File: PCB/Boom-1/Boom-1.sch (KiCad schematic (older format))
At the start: 704 parts, among them J1 NoiseIOConn, J10 Osc1HFTrackConn, J11 Osc1FiltCVConn, J12 OscFiltEnv1Conn, J13 OscFiltEnv2Conn, J14 SubFiltEnv1Conn, J15 SubFiltEnv2Conn, J16 Osc1FXConn, J17 SubFXConn, J18 Osc1FiltCVConn, J19 Osc1FiltCVConn, J2 Conn_01x07, J20 Osc2FXConn, J21 OscAmpEnvConn, J22 SubAmpEnvConn, J23 OscAmpEnvBypass, J24 SubAmpAudioBypass, J25 SubAmpEnvBypass, J26 PreFV1FXConn, J27 PowerConn, J28 FV1Conn, J29 IOConn, J3 Osc1CVConn, J4 Osc2SyncConn, J5 Osc1SyncConn, J6 Osc2ScaleConn, J7 Osc2HFTrackConn, J8 Conn_01x03, J9 Osc1ScaleConn, Q1 2N3904, SW1 SW_DIP_x04, U1 CEM3340, U10 AS3320, U11 AS3310, U12 AS3310, U13 AS3310, U14 AS3310, U15 V2164D, U16 AS3310, U17 AS3310, U18 V2164D, U19 TL074, U2 CEM3340, U20 TL074, U21 TL072, U22 TL074, U23 TL074, U24 TL072, U25 TL074, U26 TL074, U27 TL072, U28 TL074, U29 TL072, U3 4013, U30 TL074, U31 TL072, U32 TL074, U33 TL074, U34 TL074, U35 TL072, U36 TL074, U37 TL074, U38 TL072, U39 TL074, U4 NOISE, U40 TL072, U41 TL074, U42 TL074, U43 TL074, U44 TL074, U45 L7905, U46 L7805, U47 TL072, U48 TL072, U5 V2164D, U6 V2164D, U7 V2164D, U8 AS3320, U9 AS3320

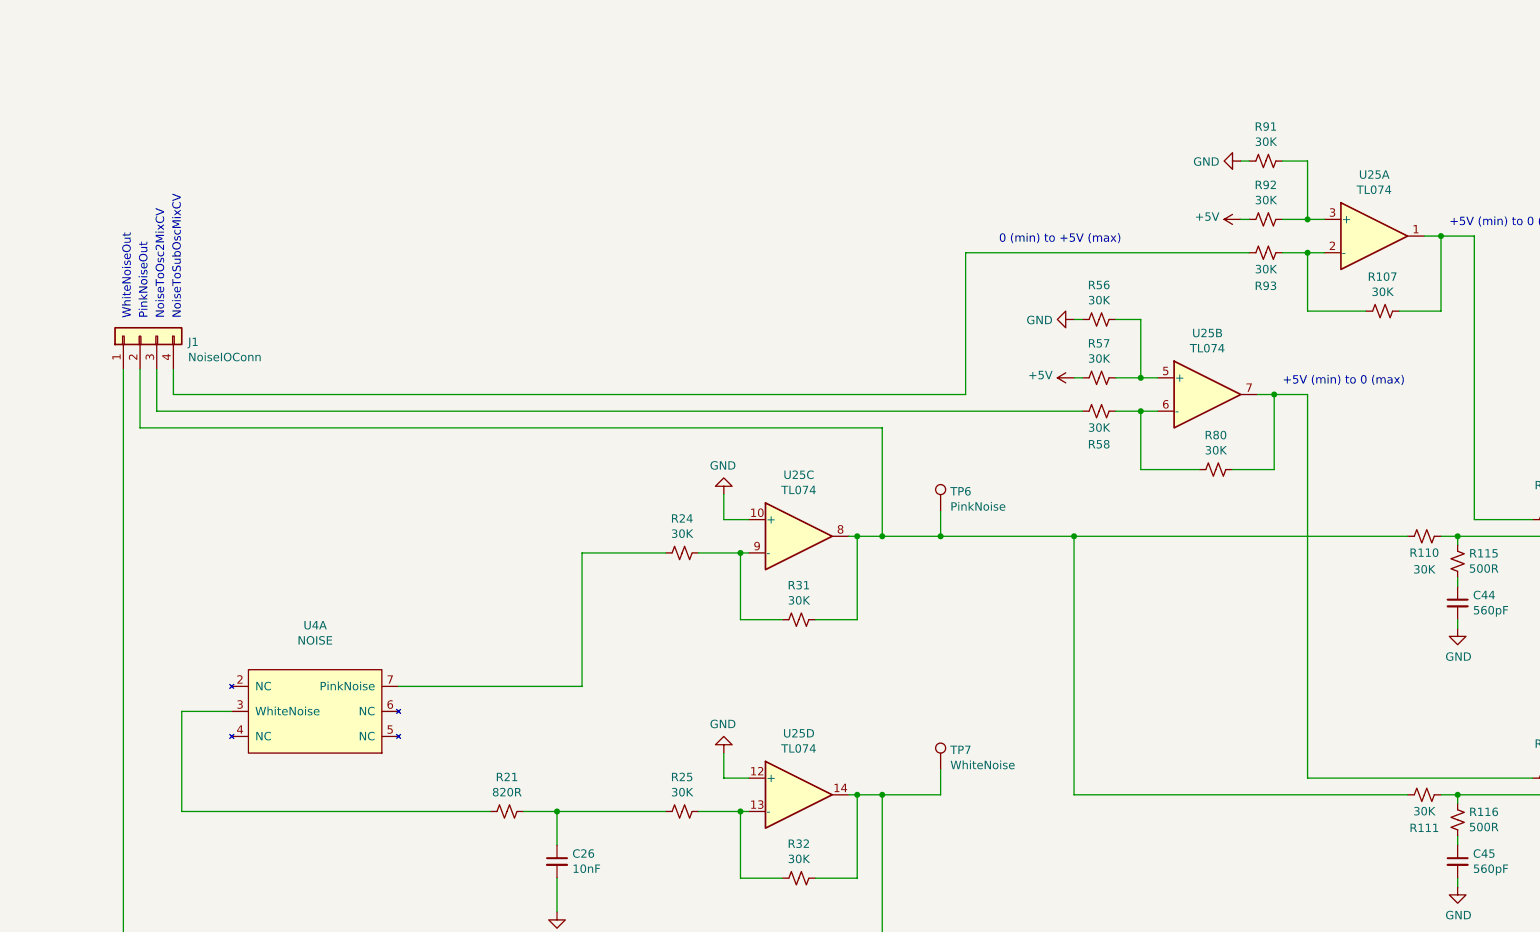
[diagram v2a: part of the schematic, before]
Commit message: compacted osc1, osc2, sub and noise
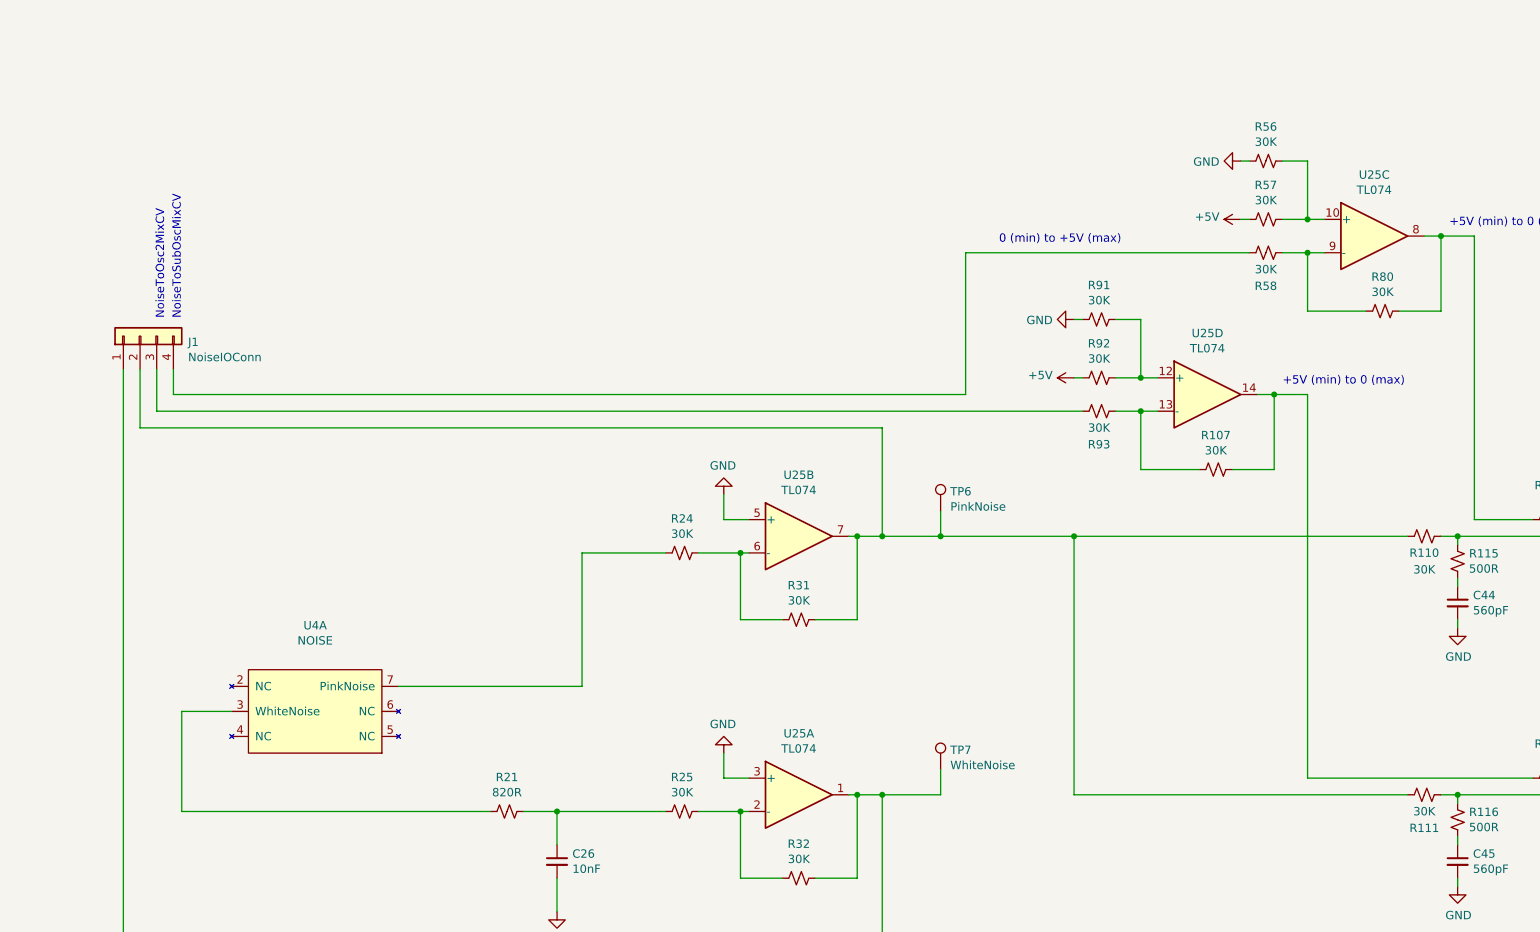
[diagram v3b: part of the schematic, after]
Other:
- note removed: "PinkNoiseOut"
- note removed: "WhiteNoiseOut"
- moved on the sheet: R107, R56, R57, R58, R80, R91, R92, R93
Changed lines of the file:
@@
 Connection ~ 10450 47750
 Wire Wire Line
-	10450 49300 10600 49300
-Wire Wire Line
 	10450 47750 10600 47750
 $Comp
@@
 Wire Wire Line
 	10600 47750 10950 47750
-Text Notes 6200 46450 1    50   ~ 0
-PinkNoiseOut
-Text Notes 6100 46450 1    50   ~ 0
-WhiteNoiseOut
 Text Notes 6300 46450 1    50   ~ 0
 NoiseToOsc2MixCV
@@
 	10550 43750 10700 43750
 Wire Wire Line
-	6050 50300 10600 50300
-Wire Wire Line
-	10600 50300 10600 49300
-Connection ~ 10600 49300
-Wire Wire Line
-	10600 49300 10950 49300
-Wire Wire Line
 	16000 47700 16500 47700
 Wire Wire Line
@@
 Wire Wire Line
 	6150 47100 10600 47100
-Wire Wire Line
-	6050 46750 6050 50300
 Text Label 35350 28950 0    50   ~ 0
 AudioOutput
@@
 	12950 46900 13150 46900
 Wire Wire Line
-	12150 46450 12150 46800
+	13150 45500 13150 45850
 Wire Wire Line
-	12150 46450 12000 46450
+	13150 45500 13000 45500
 $Comp
 L Device:R_Small_US R56
 U 1 1 770F3747
-P 11900 46450
-F 0 "R56" V 12105 46450 50  0000 C CNN
-F 1 "30K" V 12014 46450 50  0000 C CNN
-F 2 "Resistor_THT:R_Axial_DIN0207_L6.3mm_D2.5mm_P7.62mm_Horizontal" H 11900 46450 50  0001 C CNN
-F 3 "~" H 11900 46450 50  0001 C CNN
-	1    11900 46450
+P 12900 45500
+F 0 "R56" V 13105 45500 50  0000 C CNN
+F 1 "30K" V 13014 45500 50  0000 C CNN
+F 2 "Resistor_THT:R_Axial_DIN0207_L6.3mm_D2.5mm_P7.62mm_Horizontal" H 12900 45500 50  0001 C CNN
+F 3 "~" H 12900 45500 50  0001 C CNN
+	1    12900 45500
 	0    -1   -1   0
 $EndComp
 Wire Wire Line
-	12150 46800 12250 46800
-Connection ~ 12150 46800
+	13150 45850 13250 45850
+Connection ~ 13150 45850
 Wire Wire Line
 	11800 46800 11750 46800
 Wire Wire Line
-	12000 46800 12150 46800
+	13000 45850 13150 45850
 $Comp
 L Device:R_Small_US R57
 U 1 1 770F372B
-P 11900 46800
-F 0 "R57" V 12105 46800 50  0000 C CNN
-F 1 "30K" V 12014 46800 50  0000 C CNN
-F 2 "Resistor_THT:R_Axial_DIN0207_L6.3mm_D2.5mm_P7.62mm_Horizontal" H 11900 46800 50  0001 C CNN
-F 3 "~" H 11900 46800 50  0001 C CNN
-	1    11900 46800
+P 12900 45850
+F 0 "R57" V 13105 45850 50  0000 C CNN
+F 1 "30K" V 13014 45850 50  0000 C CNN
+F 2 "Resistor_THT:R_Axial_DIN0207_L6.3mm_D2.5mm_P7.62mm_Horizontal" H 12900 45850 50  0001 C CNN
+F 3 "~" H 12900 45850 50  0001 C CNN
+	1    12900 45850
 	0    -1   -1   0
 $EndComp
-Connection ~ 12150 47000
+Connection ~ 13150 46050
 Wire Wire Line
-	12000 47000 12150 47000
+	13000 46050 13150 46050
 $Comp
 L Device:R_Small_US R58
 U 1 1 770F3711
-P 11900 47000
-F 0 "R58" V 11700 47000 50  0000 C CNN
-F 1 "30K" V 11800 47000 50  0000 C CNN
-F 2 "Resistor_THT:R_Axial_DIN0207_L6.3mm_D2.5mm_P7.62mm_Horizontal" H 11900 47000 50  0001 C CNN
-F 3 "~" H 11900 47000 50  0001 C CNN
-	1    11900 47000
+P 12900 46050
+F 0 "R58" V 12700 46050 50  0000 C CNN
+F 1 "30K" V 12800 46050 50  0000 C CNN
+F 2 "Resistor_THT:R_Axial_DIN0207_L6.3mm_D2.5mm_P7.62mm_Horizontal" H 12900 46050 50  0001 C CNN
+F 3 "~" H 12900 46050 50  0001 C CNN
+	1    12900 46050
 	0    -1   -1   0
 $EndComp
 Wire Wire Line
-	12950 47350 12700 47350
+	13950 46400 13700 46400
 Wire Wire Line
 	12950 46900 12950 47350
@@
 	12850 46900 12950 46900
 Wire Wire Line
-	12150 47350 12500 47350
+	13150 46400 13500 46400
 Wire Wire Line
-	12150 47000 12150 47350
+	13150 46050 13150 46400
 Wire Wire Line
-	12250 47000 12150 47000
+	13250 46050 13150 46050
 $Comp
 L Device:R_Small_US R80
 U 1 1 770F36F3
-P 12600 47350
-F 0 "R80" V 12805 47350 50  0000 C CNN
-F 1 "30K" V 12714 47350 50  0000 C CNN
-F 2 "Resistor_THT:R_Axial_DIN0207_L6.3mm_D2.5mm_P7.62mm_Horizontal" H 12600 47350 50  0001 C CNN
-F 3 "~" H 12600 47350 50  0001 C CNN
-	1    12600 47350
+P 13600 46400
+F 0 "R80" V 13805 46400 50  0000 C CNN
+F 1 "30K" V 13714 46400 50  0000 C CNN
+F 2 "Resistor_THT:R_Axial_DIN0207_L6.3mm_D2.5mm_P7.62mm_Horizontal" H 13600 46400 50  0001 C CNN
+F 3 "~" H 13600 46400 50  0001 C CNN
+	1    13600 46400
 	0    -1   -1   0
 $EndComp
-Connection ~ 13950 45950
 Wire Wire Line
 	13950 45950 14150 45950
@@
 $EndComp
 Wire Wire Line
-	13150 45500 13150 45850
+	12150 46450 12150 46800
 Wire Wire Line
-	13150 45500 13000 45500
+	12150 46450 12000 46450
 $Comp
 L Device:R_Small_US R91
 U 1 1 770F3660
-P 12900 45500
-F 0 "R91" V 13105 45500 50  0000 C CNN
-F 1 "30K" V 13014 45500 50  0000 C CNN
-F 2 "Resistor_THT:R_Axial_DIN0207_L6.3mm_D2.5mm_P7.62mm_Horizontal" H 12900 45500 50  0001 C CNN
-F 3 "~" H 12900 45500 50  0001 C CNN
-	1    12900 45500
+P 11900 46450
+F 0 "R91" V 12105 46450 50  0000 C CNN
+F 1 "30K" V 12014 46450 50  0000 C CNN
+F 2 "Resistor_THT:R_Axial_DIN0207_L6.3mm_D2.5mm_P7.62mm_Horizontal" H 11900 46450 50  0001 C CNN
+F 3 "~" H 11900 46450 50  0001 C CNN
+	1    11900 46450
 	0    -1   -1   0
 $EndComp
 Wire Wire Line
-	13150 45850 13250 45850
-Connection ~ 13150 45850
+	12150 46800 12250 46800
+Connection ~ 12150 46800
 Wire Wire Line
 	12800 45850 12750 45850
@@
 $EndComp
 Wire Wire Line
-	13000 45850 13150 45850
+	12000 46800 12150 46800
 $Comp
 L Device:R_Small_US R92
 U 1 1 770F362E
-P 12900 45850
-F 0 "R92" V 13105 45850 50  0000 C CNN
-F 1 "30K" V 13014 45850 50  0000 C CNN
-F 2 "Resistor_THT:R_Axial_DIN0207_L6.3mm_D2.5mm_P7.62mm_Horizontal" H 12900 45850 50  0001 C CNN
-F 3 "~" H 12900 45850 50  0001 C CNN
-	1    12900 45850
+P 11900 46800
+F 0 "R92" V 12105 46800 50  0000 C CNN
+F 1 "30K" V 12014 46800 50  0000 C CNN
+F 2 "Resistor_THT:R_Axial_DIN0207_L6.3mm_D2.5mm_P7.62mm_Horizontal" H 11900 46800 50  0001 C CNN
+F 3 "~" H 11900 46800 50  0001 C CNN
+	1    11900 46800
 	0    -1   -1   0
 $EndComp
-Connection ~ 13150 46050
+Connection ~ 12150 47000
 Wire Wire Line
-	13000 46050 13150 46050
+	12000 47000 12150 47000
 $Comp
 L Device:R_Small_US R93
 U 1 1 770F3614
-P 12900 46050
-F 0 "R93" V 12700 46050 50  0000 C CNN
-F 1 "30K" V 12800 46050 50  0000 C CNN
-F 2 "Resistor_THT:R_Axial_DIN0207_L6.3mm_D2.5mm_P7.62mm_Horizontal" H 12900 46050 50  0001 C CNN
-F 3 "~" H 12900 46050 50  0001 C CNN
-	1    12900 46050
+P 11900 47000
+F 0 "R93" V 11700 47000 50  0000 C CNN
+F 1 "30K" V 11800 47000 50  0000 C CNN
+F 2 "Resistor_THT:R_Axial_DIN0207_L6.3mm_D2.5mm_P7.62mm_Horizontal" H 11900 47000 50  0001 C CNN
+F 3 "~" H 11900 47000 50  0001 C CNN
+	1    11900 47000
 	0    -1   -1   0
 $EndComp
 Wire Wire Line
-	13950 46400 13700 46400
+	12950 47350 12700 47350
 Wire Wire Line
 	13950 45950 13950 46400
 Wire Wire Line
-	13850 45950 13950 45950
-Wire Wire Line
-	13150 46400 13500 46400
+	12150 47350 12500 47350
 Wire Wire Line
-	13150 46050 13150 46400
+	12150 47000 12150 47350
 Wire Wire Line
-	13250 46050 13150 46050
+	12250 47000 12150 47000
 $Comp
 L Device:R_Small_US R107
 U 1 1 770F35F6
-P 13600 46400
-F 0 "R107" V 13805 46400 50  0000 C CNN
-F 1 "30K" V 13714 46400 50  0000 C CNN
-F 2 "Resistor_THT:R_Axial_DIN0207_L6.3mm_D2.5mm_P7.62mm_Horizontal" H 13600 46400 50  0001 C CNN
-F 3 "~" H 13600 46400 50  0001 C CNN
-	1    13600 46400
+P 12600 47350
+F 0 "R107" V 12805 47350 50  0000 C CNN
+F 1 "30K" V 12714 47350 50  0000 C CNN
+F 2 "Resistor_THT:R_Axial_DIN0207_L6.3mm_D2.5mm_P7.62mm_Horizontal" H 12600 47350 50  0001 C CNN
+F 3 "~" H 12600 47350 50  0001 C CNN
+	1    12600 47350
 	0    -1   -1   0
 $EndComp
@@
 $Comp
 L Amplifier_Operational:TL074 U25
-U 1 1 69F139BD
-P 13550 45950
-F 0 "U25" H 13550 46317 50  0000 C CNN
-F 1 "TL074" H 13550 46226 50  0000 C CNN
-F 2 "Package_DIP:DIP-14_W7.62mm" H 13500 46050 50  0001 C CNN
-F 3 "http://www.ti.com/lit/ds/symlink/tl071.pdf" H 13600 46150 50  0001 C CNN
-	1    13550 45950
-	1    0    0    -1
-$EndComp
-$Comp
-L Amplifier_Operational:TL074 U25
-U 2 1 69F1B5EF
+U 4 1 69F139BD
 P 12550 46900
 F 0 "U25" H 12550 47267 50  0000 C CNN
@@
 F 2 "Package_DIP:DIP-14_W7.62mm" H 12500 47000 50  0001 C CNN
 F 3 "http://www.ti.com/lit/ds/symlink/tl071.pdf" H 12600 47100 50  0001 C CNN
-	2    12550 46900
+	4    12550 46900
+	1    0    0    -1
+$EndComp
+$Comp
+L Amplifier_Operational:TL074 U25
+U 3 1 69F1B5EF
+P 13550 45950
+F 0 "U25" H 13550 46317 50  0000 C CNN
+F 1 "TL074" H 13550 46226 50  0000 C CNN
+F 2 "Package_DIP:DIP-14_W7.62mm" H 13500 46050 50  0001 C CNN
+F 3 "http://www.ti.com/lit/ds/symlink/tl071.pdf" H 13600 46150 50  0001 C CNN
+	3    13550 45950
 	1    0    0    -1
 $EndComp
 $Comp
 L Amplifier_Operational:TL074 U25
-U 3 1 69F235EB
+U 2 1 69F235EB
 P 10100 47750
 F 0 "U25" H 10100 48117 50  0000 C CNN
@@
 F 2 "Package_DIP:DIP-14_W7.62mm" H 10050 47850 50  0001 C CNN
 F 3 "http://www.ti.com/lit/ds/symlink/tl071.pdf" H 10150 47950 50  0001 C CNN
-	3    10100 47750
+	2    10100 47750
 	1    0    0    -1
 $EndComp
 $Comp
 L Amplifier_Operational:TL074 U25
-U 4 1 69F2BE9E
+U 1 1 69F2BE9E
 P 10100 49300
 F 0 "U25" H 10100 49667 50  0000 C CNN
@@
 F 2 "Package_DIP:DIP-14_W7.62mm" H 10050 49400 50  0001 C CNN
 F 3 "http://www.ti.com/lit/ds/symlink/tl071.pdf" H 10150 49500 50  0001 C CNN
-	4    10100 49300
+	1    10100 49300
 	1    0    0    -1
 $EndComp
@@
 Wire Wire Line
 	12850 32900 12850 35250
+Wire Wire Line
+	10600 49300 10950 49300
+Wire Wire Line
+	10450 49300 10600 49300
+Connection ~ 10600 49300
+Wire Wire Line
+	10600 50300 10600 49300
+Wire Wire Line
+	6050 50300 10600 50300
+Wire Wire Line
+	6050 46750 6050 50300
+Wire Wire Line
+	13850 45950 13950 45950
+Connection ~ 13950 45950
 $EndSCHEMATC

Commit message: osc2 filt layout WITHOUT VIA .. BOOM
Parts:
- removed J19: Osc1FiltCVConn, Connector_PinHeader_2.54mm:PinHeader_1x02_P2.54mm_Vertical, symbol Connector_Generic:Conn_01x02
- removed J20: Osc2FXConn, Connector_PinHeader_2.54mm:PinHeader_1x05_P2.54mm_Vertical, symbol Connector_Generic:Conn_01x05
- removed U30: TL074, Package_DIP:DIP-14_W7.62mm, symbol Amplifier_Operational:TL074
- added C180, C181: 100nF, Capacitor_THT:C_Disc_D5.0mm_W2.5mm_P5.00mm, symbol Device:C_Small
- added J20: Osc2FXConn, Connector_PinHeader_2.54mm:PinHeader_1x07_P2.54mm_Vertical, symbol Connector_Generic:Conn_01x07
- added U30, U49: TL072, Package_DIP:DIP-8_W7.62mm, symbol Amplifier_Operational:TL072
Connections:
- wire segments 3049 -> 3061

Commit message: updated conns on osc1 and sub filt to match osc2 filt
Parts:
- removed J11, J18: Osc1FiltCVConn, Connector_PinHeader_2.54mm:PinHeader_1x02_P2.54mm_Vertical, symbol Connector_Generic:Conn_01x02
- removed J16: Osc1FXConn, Connector_PinHeader_2.54mm:PinHeader_1x05_P2.54mm_Vertical, symbol Connector_Generic:Conn_01x05
- removed J17: SubFXConn, Connector_PinHeader_2.54mm:PinHeader_1x05_P2.54mm_Vertical, symbol Connector_Generic:Conn_01x05
- added J11: SubFiltConn, Connector_PinHeader_2.54mm:PinHeader_1x07_P2.54mm_Vertical, symbol Connector_Generic:Conn_01x07
- added J16: Osc1FiltConn, Connector_PinHeader_2.54mm:PinHeader_1x07_P2.54mm_Vertical, symbol Connector_Generic:Conn_01x07
- J20: value Osc2FXConn -> Osc2FiltConn
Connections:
- wire segments 3061 -> 3065
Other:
- moved on the sheet: TP27, TP30

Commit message: almost done with a filt env layout
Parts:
- removed J12: OscFiltEnv1Conn, Connector_PinHeader_2.54mm:PinHeader_1x10_P2.54mm_Vertical, symbol Connector_Generic:Conn_01x10
- added J12: OscFiltEnv1Conn, Connector_PinHeader_2.54mm:PinHeader_1x05_P2.54mm_Vertical, symbol Connector_Generic:Conn_01x05
- added J17: OscFiltEnv1CVConn, Connector_PinHeader_2.54mm:PinHeader_1x04_P2.54mm_Vertical, symbol Connector_Generic:Conn_01x04
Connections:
- no-connect marks 19 -> 18
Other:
- moved on the sheet: U27A, U27B
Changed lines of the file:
@@
 Text Notes 20750 21100 3    50   ~ 0
 OscFiltEnv1Trigger
-Text Notes 20850 21100 3    50   ~ 0
+Text Notes 20900 21100 3    50   ~ 0
 OscFiltEnv1AttackCV
-Text Notes 20950 21100 3    50   ~ 0
+Text Notes 21000 21100 3    50   ~ 0
 OscFiltEnv1DecayCV
-Text Notes 21050 21100 3    50   ~ 0
+Text Notes 21100 21100 3    50   ~ 0
 OscFiltEnv1SustainCV
-Text Notes 21150 21100 3    50   ~ 0
+Text Notes 21200 21100 3    50   ~ 0
 OscFiltEnv1ReleaseCV
-$Comp
-L Connector_Generic:Conn_01x10 J12
-U 1 1 732F368F
-P 20750 21000
-F 0 "J12" V 20800 20350 50  0000 C CNN
-F 1 "OscFiltEnv1Conn" V 20700 20100 50  0000 C CNN
-F 2 "Connector_PinHeader_2.54mm:PinHeader_1x10_P2.54mm_Vertical" H 20750 21000 50  0001 C CNN
-F 3 "~" H 20750 21000 50  0001 C CNN
-	1    20750 21000
-	0    -1   1    0
-$EndComp
-NoConn ~ 21250 20800
 Wire Wire Line
 	20850 27050 20850 27700
@@
 L Amplifier_Operational:TL072 U27
 U 1 1 601065A4
-P 21750 19300
-F 0 "U27" H 21750 19667 50  0000 C CNN
-F 1 "TL072" H 21750 19576 50  0000 C CNN
-F 2 "Package_DIP:DIP-8_W7.62mm" H 21750 19300 50  0001 C CNN
-F 3 "http://www.ti.com/lit/ds/symlink/tl071.pdf" H 21750 19300 50  0001 C CNN
-	1    21750 19300
-	1    0    0    -1
-$EndComp
-$Comp
-L Amplifier_Operational:TL072 U27
-U 2 1 601145C9
 P 22350 19800
 F 0 "U27" H 22350 20167 50  0000 C CNN
@@
 F 2 "Package_DIP:DIP-8_W7.62mm" H 22350 19800 50  0001 C CNN
 F 3 "http://www.ti.com/lit/ds/symlink/tl071.pdf" H 22350 19800 50  0001 C CNN
-	2    22350 19800
+	1    22350 19800
+	1    0    0    -1
+$EndComp
+$Comp
+L Amplifier_Operational:TL072 U27
+U 2 1 601145C9
+P 21750 19300
+F 0 "U27" H 21750 19667 50  0000 C CNN
+F 1 "TL072" H 21750 19576 50  0000 C CNN
+F 2 "Package_DIP:DIP-8_W7.62mm" H 21750 19300 50  0001 C CNN
+F 3 "http://www.ti.com/lit/ds/symlink/tl071.pdf" H 21750 19300 50  0001 C CNN
+	2    21750 19300
 	1    0    0    -1
 $EndComp
@@
 Wire Wire Line
 	22500 11950 22500 13750
+$Comp
+L Connector_Generic:Conn_01x05 J12
+U 1 1 60DA4F70
+P 20550 21000
+F 0 "J12" V 20400 21350 50  0000 R CNN
+F 1 "OscFiltEnv1Conn" V 20500 21900 50  0000 R CNN
+F 2 "Connector_PinHeader_2.54mm:PinHeader_1x05_P2.54mm_Vertical" H 20550 21000 50  0001 C CNN
+F 3 "~" H 20550 21000 50  0001 C CNN
+	1    20550 21000
+	0    -1   1    0
+$EndComp
+$Comp
+L Connector_Generic:Conn_01x04 J17
+U 1 1 60DB7A00
+P 20950 21000
+F 0 "J17" V 20822 20712 50  0000 R CNN
+F 1 "OscFiltEnv1CVConn" V 20913 20712 50  0000 R CNN
+F 2 "Connector_PinHeader_2.54mm:PinHeader_1x04_P2.54mm_Vertical" H 20950 21000 50  0001 C CNN
+F 3 "~" H 20950 21000 50  0001 C CNN
+	1    20950 21000
+	0    -1   1    0
+$EndComp
 $EndSCHEMATC
